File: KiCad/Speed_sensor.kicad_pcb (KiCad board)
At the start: 2 copper layers, 70 parts, among them J1 USB_B_Micro, J2 SWD, U1 BQ24040DSQR, U2 TP1941U, U3 ST1PS02, U4 nRF52832-QFxx, U5 LIS2DH12, Y1 32,768kHz, Y2 32MHz

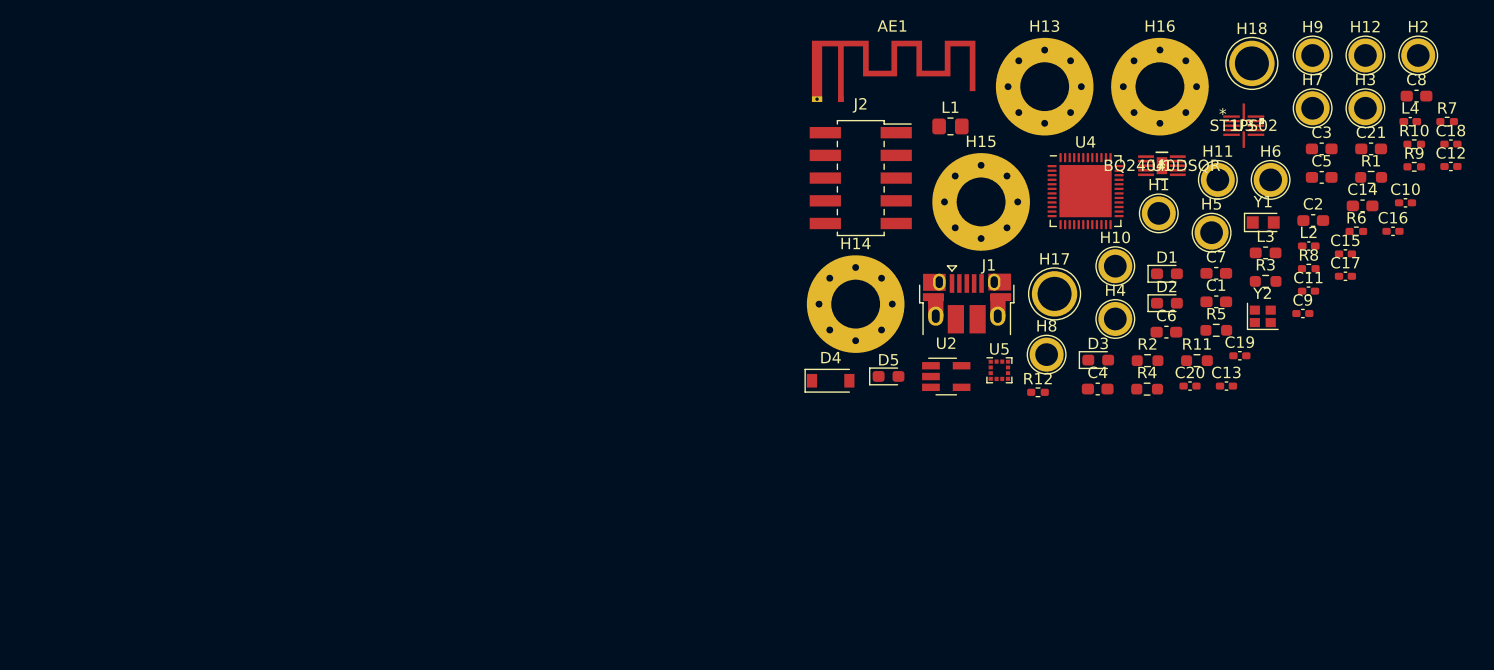
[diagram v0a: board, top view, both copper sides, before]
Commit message: custom footprints von Manu übernommen (jetzt sollte alles passen), PCB layout angefangen.
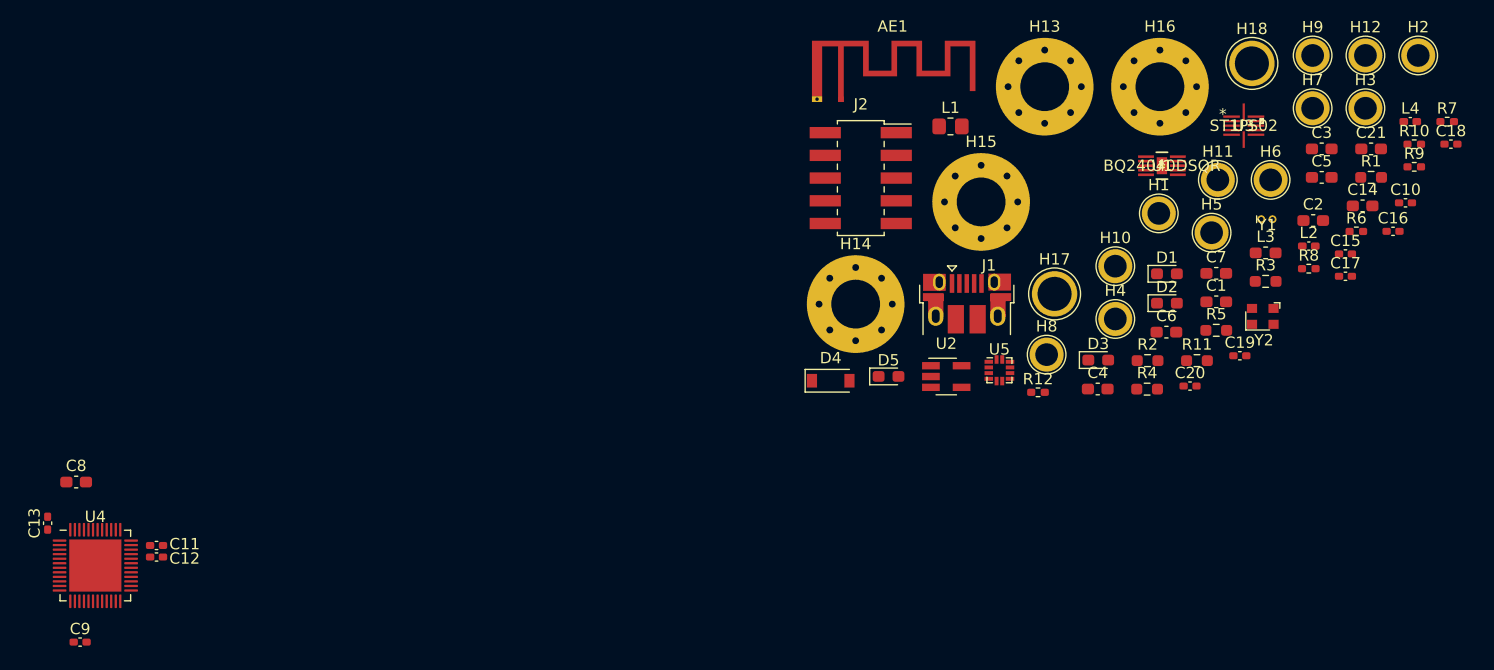
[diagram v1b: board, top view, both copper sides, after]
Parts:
- U4: footprint Package_DFN_QFN:QFN-48-1EP_6x6mm_P0.4mm_EP4.6x4.6mm -> myparts:QFN-48-1EP_6x6mm_P0.4mm_EP4.6x4.6mm_Handsolder
- U5: footprint Package_LGA:LGA-12_2x2mm_P0.5mm -> myparts:LGA-12_2x2mm_P0.5mm_Handsolder
- Y1: footprint Crystal:Crystal_SMD_2012-2Pin_2.0x1.2mm_HandSoldering -> myparts:TestPoint_2Pads_Pitch1mm_Drill0.4mm
- Y2: footprint Crystal:Crystal_SMD_2016-4Pin_2.0x1.6mm -> myparts:SMD-2016_4P
- moved C8 122.9 mm to (156.6, 56.9)
- moved C12 119.1 mm to (163.6, 63.5)
- moved C9 111.5 mm to (156.9, 71.0)
- moved C13 104.5 mm to (154.1, 60.5), turned to 90 degrees
- moved C11 103.9 mm to (163.6, 62.5)
- moved U4 93.2 mm to (158.3, 64.2)
- moved Y1 0.43 mm to (261.4, 33.7)

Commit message: layout update (Bauteile um den nrf grob positioniert)
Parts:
- moved C16 127.3 mm to (149.3, 66.7)
- moved C15 121.6 mm to (149.4, 62.0)
- moved Y1 116.7 mm to (148.8, 64.5), turned to 270 degrees
- moved C10 114.8 mm to (162.4, 60.6), turned to 90 degrees
- moved C14 114.1 mm to (158.8, 58.3), turned to 270 degrees
- moved L4 113.3 mm to (168.2, 65.7), turned to 180 degrees
- moved C18 113.2 mm to (170.1, 62.4)
- moved C17 108.2 mm to (163.6, 65.8), turned to 270 degrees
- moved L2 107.9 mm to (159.0, 55.4)
- moved L3 106.1 mm to (157.1, 56.6), turned to 90 degrees
- moved Y2 92.7 mm to (170.1, 60.4)
- moved C19 89.9 mm to (170.1, 58.4), turned to 180 degrees
- moved AE1 63.8 mm to (180.3, 69.7)
- moved C9 3.50 mm to (154.5, 68.5), turned to 180 degrees
- moved C8 2.88 mm to (154.7, 59.1), turned to 180 degrees
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
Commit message: parts of power circuit roughly layouted, again
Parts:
- moved R1 155.5 mm to (122.8, 78.2), turned to 90 degrees
- moved H18 148.4 mm to (140.1, 107.3)
- moved C2 138.7 mm to (140.6, 94.0), turned to 180 degrees
- moved D1 137.3 mm to (122.8, 83.2), turned to 270 degrees
- moved R7 136.8 mm to (160.1, 95.7), turned to 270 degrees
- moved U1 132.1 mm to (138.9, 97.0)
- moved C21 131.5 mm to (149.6, 79.0), turned to 180 degrees
- moved C1 131.0 mm to (137.2, 94.0)
- moved J1 129.4 mm to (115.7, 91.2), turned to 270 degrees
- moved R9 129.3 mm to (163.0, 94.9), turned to 180 degrees
- moved C3 129.3 mm to (154.3, 92.2)
- moved D2 128.5 mm to (138.3, 99.8)
- moved R3 128.3 mm to (145.6, 94.5), turned to 180 degrees
- moved H17 128.1 mm to (133.6, 107.3)
- moved R2 127.0 mm to (134.0, 95.8), turned to 180 degrees
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
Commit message: layout. parts roughly put into the right spot
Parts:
- removed the C3 at (154.3, 92.2)
- moved H7 175.4 mm to (96.8, 71.9), turned to 90 degrees
- moved H6 169.2 mm to (96.8, 67.8), turned to 90 degrees
- moved H5 162.4 mm to (96.8, 63.8), turned to 90 degrees
- moved H13 159.6 mm to (99.6, 94.4)
- moved H4 155.9 mm to (96.8, 80.0), turned to 90 degrees
- moved H8 148.4 mm to (96.8, 75.9), turned to 90 degrees
- moved H2 148.3 mm to (127.6, 37.5)
- moved H3 139.1 mm to (131.6, 37.5)
- moved H12 134.7 mm to (136.7, 37.5)
- moved H1 128.5 mm to (123.5, 37.5)
- moved C4 127.9 mm to (139.8, 49.0), turned to 270 degrees
- moved R10 126.2 mm to (150.1, 48.6), turned to 270 degrees
- moved H14 125.7 mm to (99.6, 40.5)
- moved H9 118.8 mm to (148.1, 37.5)
- moved H11 116.9 mm to (140.5, 37.5)
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- renumbered C4 to C3, C5 to C4

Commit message: played around with part positioning slightly
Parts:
- removed H2: Vout2, TestPoint:TestPoint_Plated_Hole_D2.0mm
- added C5: 100n, Capacitor_SMD:C_0402_1005Metric_Pad0.74x0.62mm_HandSolder, F.Cu at (126.1, 80.6)
- AE1: value Antenna -> 2,4GHz
- H1, H10, H11, H12, H3, H4, H5, H6, H7, H8, H9: footprint TestPoint:TestPoint_Plated_Hole_D2.0mm -> TestPoint:TestPoint_Loop_D1.80mm_Drill1.0mm_Beaded
- moved C7 44.7 mm to (107.0, 76.2)
- moved R10 44.7 mm to (114.0, 75.1)
- moved R11 44.7 mm to (106.2, 78.8)
- moved R12 44.7 mm to (110.4, 78.4)
- moved U3 44.7 mm to (109.6, 73.9)
- moved C4 44.7 mm to (103.8, 75.5)
- moved C6 44.7 mm to (110.5, 77.0)
- moved D5 44.7 mm to (107.8, 78.8)
- moved L1 44.7 mm to (106.0, 72.8)
- moved H5 32.3 mm to (105.9, 94.7), turned to 180 degrees
- moved H6 29.9 mm to (109.7, 94.7), turned to 180 degrees
- moved H4 28.7 mm to (121.4, 94.7), turned to 180 degrees
- moved H7 28.3 mm to (113.5, 94.7), turned to 180 degrees
- moved H8 28.0 mm to (117.5, 94.7), turned to 180 degrees
- moved D4 25.8 mm to (104.4, 65.7)
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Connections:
- AE1 pad 2: (no net) -> BQ_VSS

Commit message: small changes in the layout
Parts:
- AE1: value 2,4GHz -> 2450AT18D0100E; footprint RF_Antenna:Texas_SWRA117D_2.4GHz_Right -> myparts:2450AT18D0100E
- moved H4 9.40 mm to (121.4, 85.3)
- moved H5 9.40 mm to (105.9, 85.3)
- moved H6 9.40 mm to (109.7, 85.3)
- moved H7 9.40 mm to (113.5, 85.3)
- moved H8 9.40 mm to (117.5, 85.3)
- moved H13 9.40 mm to (98.6, 85.1)
- moved H16 9.40 mm to (144.5, 85.1)
- moved J2 9.40 mm to (132.3, 81.3)
- moved C21 4.36 mm to (121.9, 78.2)
- moved C20 4.36 mm to (119.9, 77.1)
- moved U5 4.36 mm to (122.0, 74.8)
- moved C5 4.03 mm to (123.4, 77.6), turned to 270 degrees
- moved H1 3.15 mm to (118.6, 40.7)
- moved H10 3.15 mm to (133.9, 40.6)
- moved H11 3.15 mm to (130.0, 40.6)
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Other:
- copper layers 2 -> 4

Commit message: layout part placement (again, very small changes)
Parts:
- Y1: footprint myparts:TestPoint_2Pads_Pitch1mm_Drill0.4mm -> Crystal:Crystal_SMD_G8-2Pin_3.2x1.5mm
- moved L1 10.9 mm to (101.0, 63.1)
- moved C4 10.9 mm to (98.7, 65.8)
- moved C6 10.9 mm to (105.4, 67.3)
- moved C7 10.9 mm to (101.9, 66.5)
- moved D5 10.9 mm to (102.7, 69.1)
- moved R10 10.9 mm to (108.5, 65.3)
- moved R12 10.9 mm to (105.3, 68.7)
- moved U3 10.9 mm to (104.5, 64.3)
- moved R11 10.9 mm to (101.1, 69.1)
- moved C21 10.3 mm to (114.4, 71.1), turned to 180 degrees
- moved C5 9.81 mm to (115.0, 72.6), turned to 180 degrees
- moved C20 9.20 mm to (115.4, 69.1), turned to 90 degrees
- moved H13 7.11 mm to (98.6, 78.0)
- moved H16 7.11 mm to (144.5, 78.0)
- moved H4 7.11 mm to (121.4, 78.2)
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
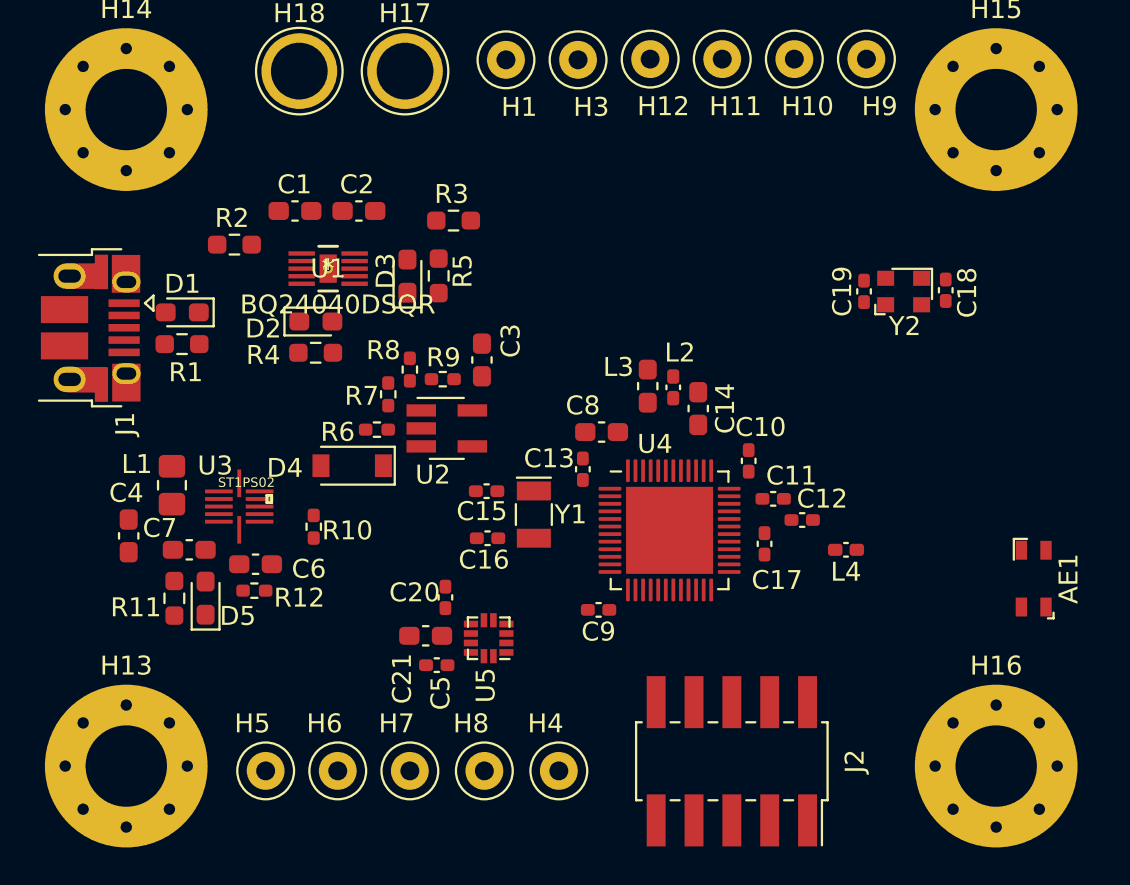
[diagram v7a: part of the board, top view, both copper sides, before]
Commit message: changed some labels in the .sch so all power stuff is labeled correctly
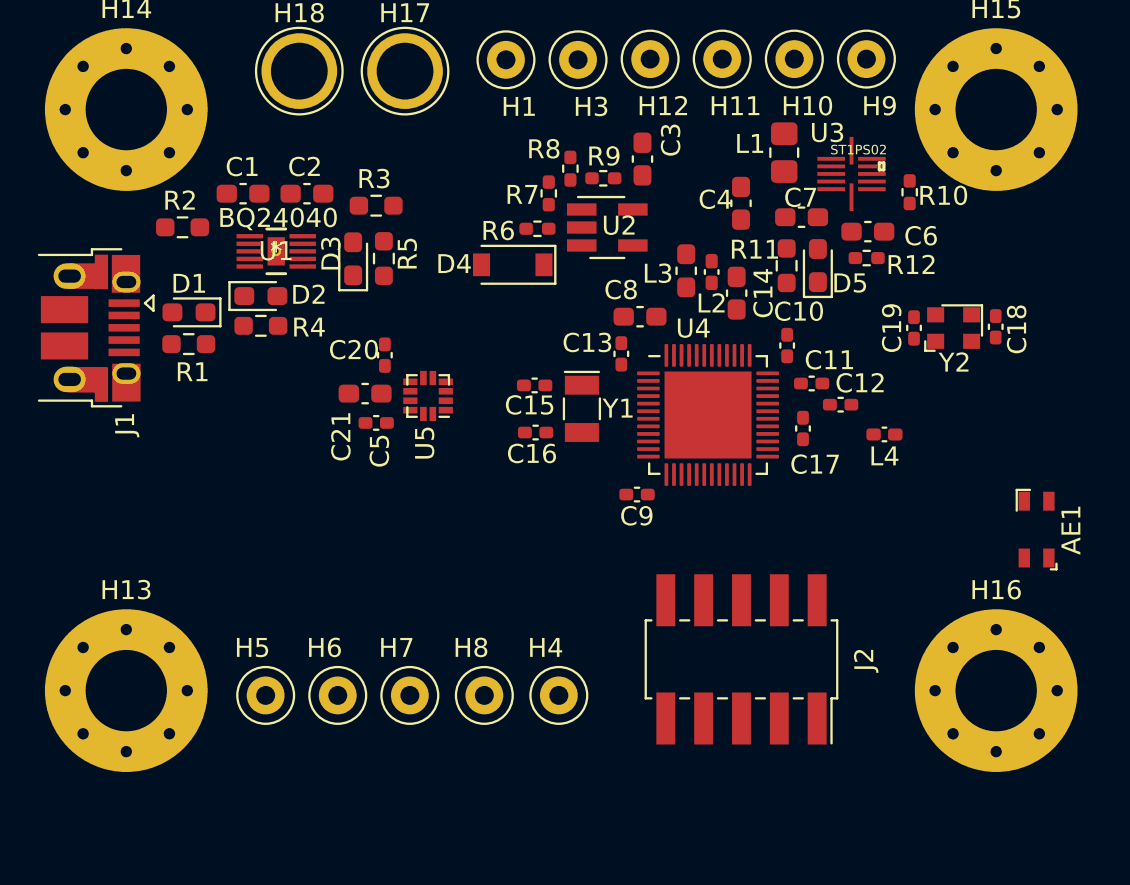
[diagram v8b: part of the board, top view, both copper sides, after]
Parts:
- U1: value BQ24040DSQR -> BQ24040
- moved C7 36.8 mm to (134.2, 49.0)
- moved R11 36.8 mm to (133.5, 51.5)
- moved R12 36.8 mm to (137.7, 51.1)
- moved C4 36.8 mm to (131.0, 48.2)
- moved C6 36.8 mm to (137.7, 49.7)
- moved D5 36.8 mm to (135.1, 51.5)
- moved L1 36.8 mm to (133.3, 45.6)
- moved U3 36.8 mm to (136.9, 46.7)
- moved R10 36.1 mm to (140.0, 47.7)
- moved R7 13.6 mm to (120.9, 47.7)
- moved R8 13.6 mm to (122.0, 46.4)
- moved R9 13.6 mm to (123.8, 46.9)
- moved U2 13.6 mm to (124.0, 49.5)
- moved C3 13.6 mm to (125.8, 45.9)
- moved D4 13.6 mm to (119.0, 51.5)
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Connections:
- net BQ_OUT renamed +BATT
- net BQ_VSS renamed GND
- net BUCK_VOUT renamed +3V0
